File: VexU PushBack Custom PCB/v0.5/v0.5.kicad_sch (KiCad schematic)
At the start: 47 parts, among them J1 Conn_01x04_Pin, J2 4P4C, J3 Conn_01x04_Pin, J4 USB_B_Micro, SW1 SW_SPDT, U1 STM32G431RBT6, U2 MP2338GTL-P, U3 MAX485E, Y1 16MHz

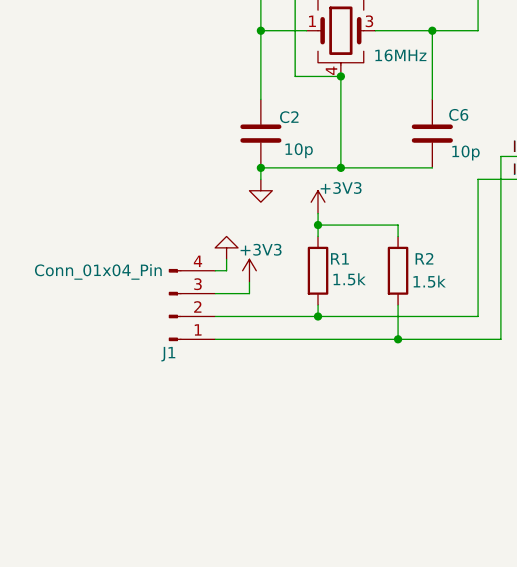
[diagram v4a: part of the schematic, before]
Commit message: Added SparkFun Library
Switched 1mm 1x4 connect out for QWIIC connector
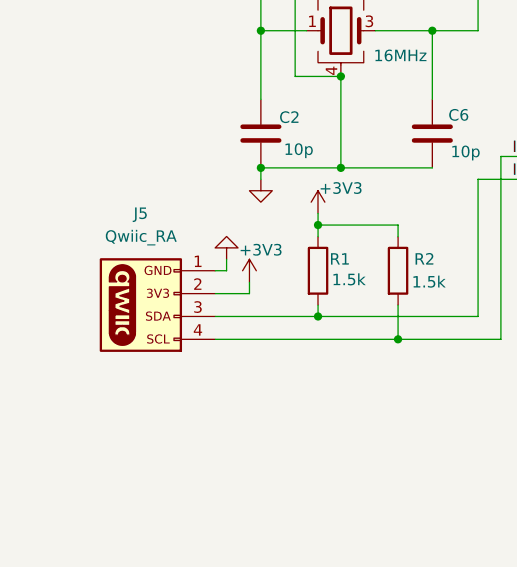
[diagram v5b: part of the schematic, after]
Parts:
- removed J1: Conn_01x04_Pin, Connector_PinHeader_2.54mm:PinHeader_1x04_P2.54mm_Horizontal, symbol Connector:Conn_01x04_Pin
- added J5: Qwiic_RA, SparkFun-Connector:JST_1x04_P1.0mm_Horizontal_SMD, symbol SparkFun-Connector:Qwiic_Horizontal
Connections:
- net +3V3: now also J5.2 (Pin_2)
- net Earth: now also J5.1 (Pin_1)
- net I2C3_SCL: now also J5.4 (Pin_4)
- net I2C3_SDA: now also J5.3 (Pin_3)
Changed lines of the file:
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@@
 	)
 	(symbol
+		(lib_id "SparkFun-Connector:Qwiic_Horizontal")
+		(at 30.48 162.56 180)
+		(unit 1)
+		(exclude_from_sim no)
+		(in_bom yes)
+		(on_board yes)
+		(dnp no)
+		(fields_autoplaced yes)
+		(property "Reference" "J5"
+			(at 27.305 151.13 0)
+			(effects
+				(font
+					(size 1.27 1.27)
+				)
+			)
+		)
+		(property "Value" "Qwiic_RA"
+			(at 27.305 153.67 0)
+			(effects
+				(font
+					(size 1.27 1.27)
+				)
+			)
+		)
+		(property "Footprint" "SparkFun-Connector:JST_1x04_P1.0mm_Horizontal_SMD"
+			(at 30.48 149.86 0)
+			(effects
+				(font
+					(size 1.27 1.27)
+				)
+				(hide yes)
+			)
+		)
+		(property "Datasheet" "https://www.jst-mfg.com/product/pdf/eng/eSH.pdf"
+			(at 30.48 147.32 0)
+			(effects
+				(font
+					(size 1.27 1.27)
+				)
+				(hide yes)
+			)
+		)
+		(property "Description" "4 pin JST 1mm polarized connector for I2C"
+			(at 30.48 144.78 0)
+			(effects
+				(font
+					(size 1.27 1.27)
+				)
+				(hide yes)
+			)
+		)
+		(property "PROD_ID" "CONN-13694"
+			(at 30.48 152.4 0)
+			(effects
+				(font
+					(size 1.27 1.27)
+				)
+				(hide yes)
+			)
+		)
+		(pin "NC1"
+		)
+		(pin "4"
+		)
+		(pin "3"
+		)
+		(pin "2"
+		)
+		(pin "NC2"
+		)
+		(pin "1"
+		)
+		(instances
+			(project ""
+				(path "/a29a069e-e320-4c99-b39c-726cf56ff93e"
+					(reference "J5")
+					(unit 1)
+				)
+			)
+		)
+	)
+	(symbol
 		(lib_id "power:+3.3VA")
 		(at 104.14 82.55 0)
@@
 					(unit 1)
 				)
-			)
-		)
-	)
-	(symbol
-		(lib_id "Connector:Conn_01x04_Pin")
-		(at 30.48 162.56 0)
-		(mirror x)
-		(unit 1)
-		(exclude_from_sim no)
-		(in_bom yes)
-		(on_board yes)
-		(dnp no)
-		(property "Reference" "J1"
-			(at 30.48 166.624 0)
-			(effects
-				(font
-					(size 1.27 1.27)
-				)
-			)
-		)
-		(property "Value" "Conn_01x04_Pin"
-			(at 22.606 157.48 0)
-			(effects
-				(font
-					(size 1.27 1.27)
-				)
-			)
-		)
-		(property "Footprint" "Connector_PinHeader_2.54mm:PinHeader_1x04_P2.54mm_Horizontal"
-			(at 30.48 162.56 0)
-			(effects
-				(font
-					(size 1.27 1.27)
-				)
-				(hide yes)
-			)
-		)
-		(property "Datasheet" "~"
-			(at 30.48 162.56 0)
-			(effects
-				(font
-					(size 1.27 1.27)
-				)
-				(hide yes)
-			)
-		)
-		(property "Description" "Generic connector, single row, 01x04, script generated"
-			(at 30.48 162.56 0)
-			(effects
-				(font
-					(size 1.27 1.27)
-				)
-				(hide yes)
-			)
-		)
-		(pin "3"
-		)
-		(pin "2"
-		)
-		(pin "1"
-		)
-		(pin "4"
-		)
-		(instances
-			(project ""
-				(path "/a29a069e-e320-4c99-b39c-726cf56ff93e"
-					(reference "J1")
-					(unit 1)
-				)
